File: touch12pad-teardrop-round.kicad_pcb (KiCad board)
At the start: 2 copper layers, 158.8 x 33 mm, 38 parts, among them J1 Conn_01x01_Female, J10 Conn_01x01_Female, J11 Conn_01x01_Female, J12 Conn_01x01_Female, J13 Conn_01x01_Female, J14 Conn_01x01_Female, J15 Conn_01x01_Female, J16 Conn_01x01_Female, J17 Conn_01x01_Female, J18 Conn_01x01_Female, J19 Conn_01x01_Female, J2 Conn_01x01_Female, J20 Conn_01x01_Female, J21 Conn_01x01_Female, J22 Conn_01x01_Female, J23 Conn_01x01_Female, J24 Conn_01x01_Female, J3 Conn_01x01_Female, J4 \, J5 Conn_01x01_Female, J6 Conn_01x01_Female, J7 Conn_01x01_Female, J8 Conn_01x01_Female, J9 Conn_01x01_Female

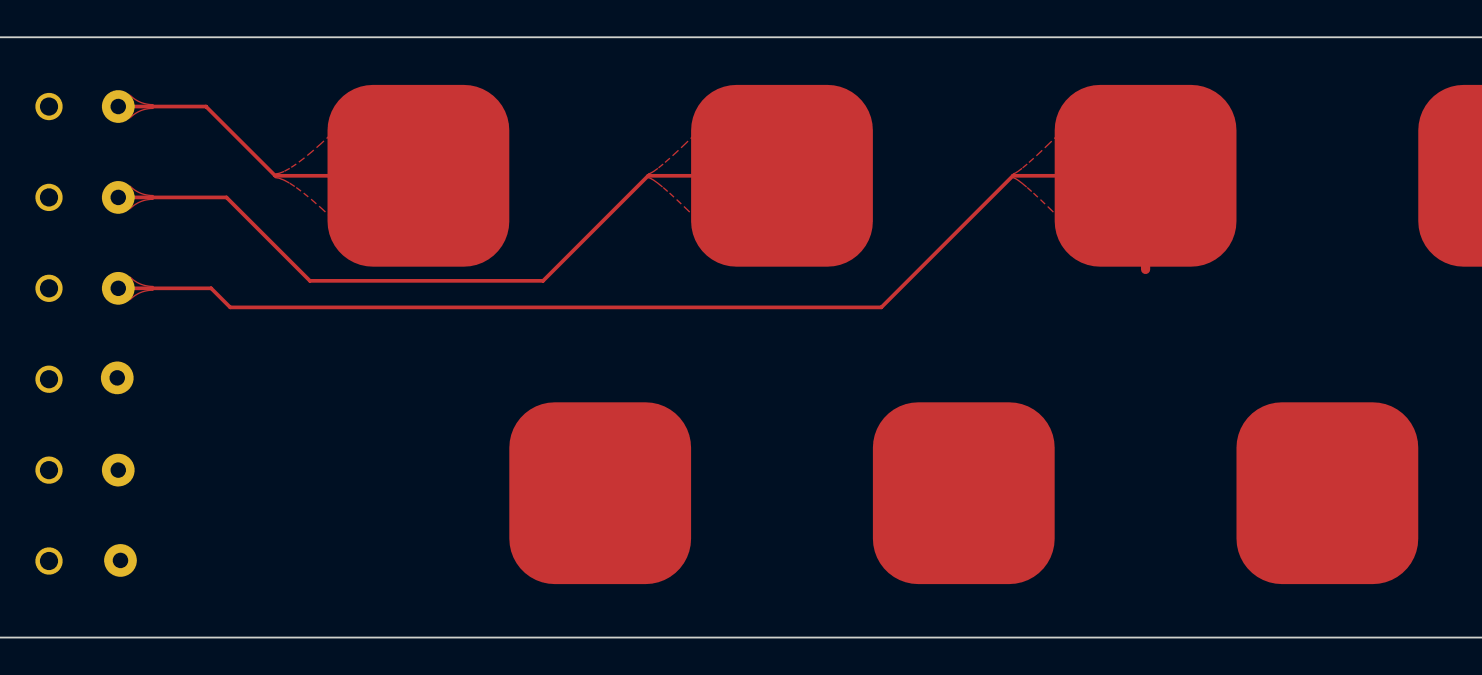
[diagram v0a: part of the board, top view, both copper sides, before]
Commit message: start re-routing flex touch board
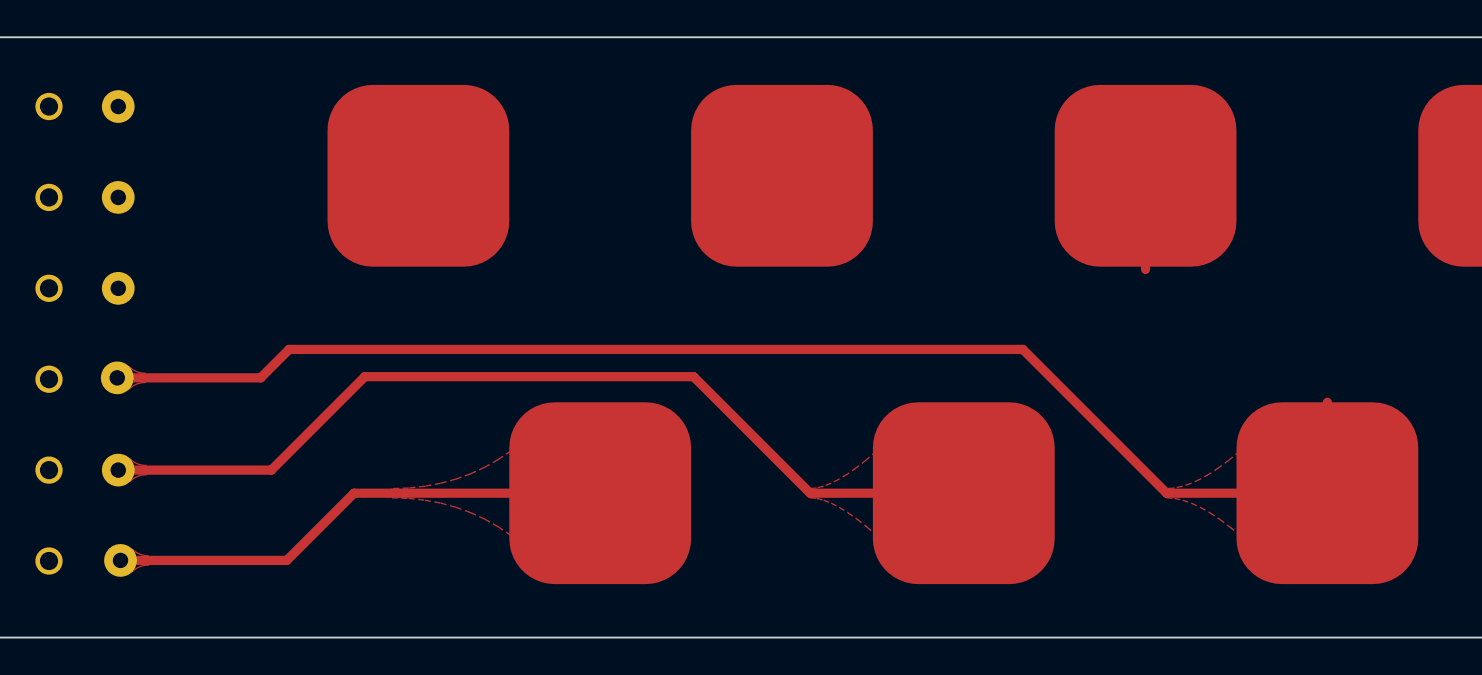
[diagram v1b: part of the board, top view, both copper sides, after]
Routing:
- net Net-(J12-Pad1): track 0.00 -> 75.5 mm
- net Net-(J9-Pad1): track 65.1 -> 5.15 mm
- net Net-(J11-Pad1): track 0.00 -> 51.3 mm
- net Net-(J8-Pad1): track 40.8 -> 0.00 mm
- net Net-(J10-Pad1): track 0.00 -> 27.9 mm
- net Net-(J1-Pad1): track 18.1 -> 0.04 mm
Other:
- net class Default: clearance 0.1524 -> 0.508; trace_width 0.1524 -> 0.508
- net class trace: clearance 0.254 -> 0.508
- rule trace_clearance: 0.1524 -> 0.508

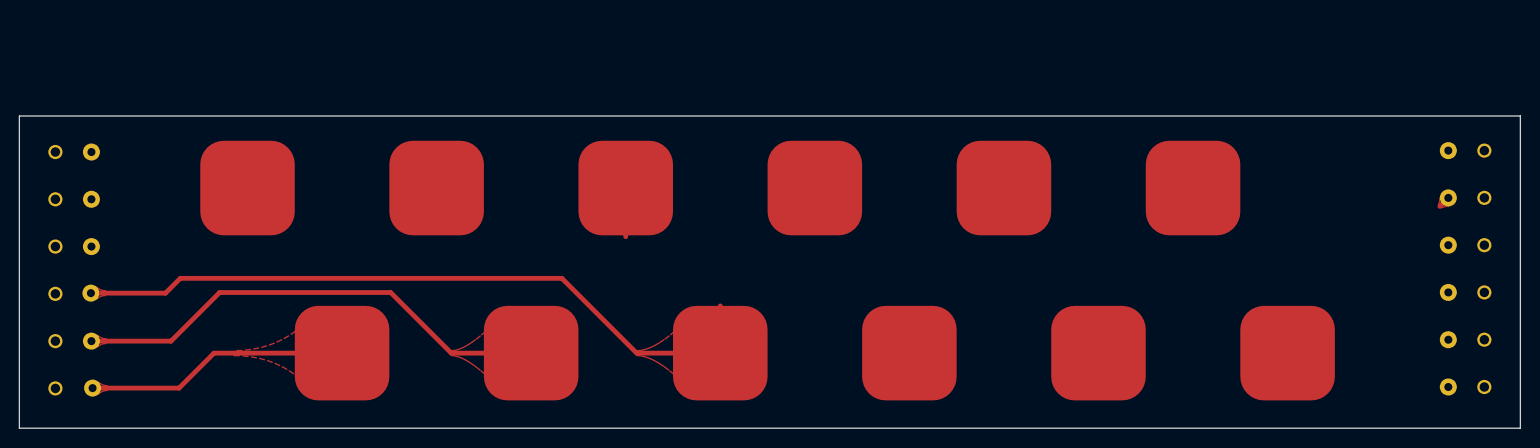
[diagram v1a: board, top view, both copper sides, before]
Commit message: add rounded tracks using plugin
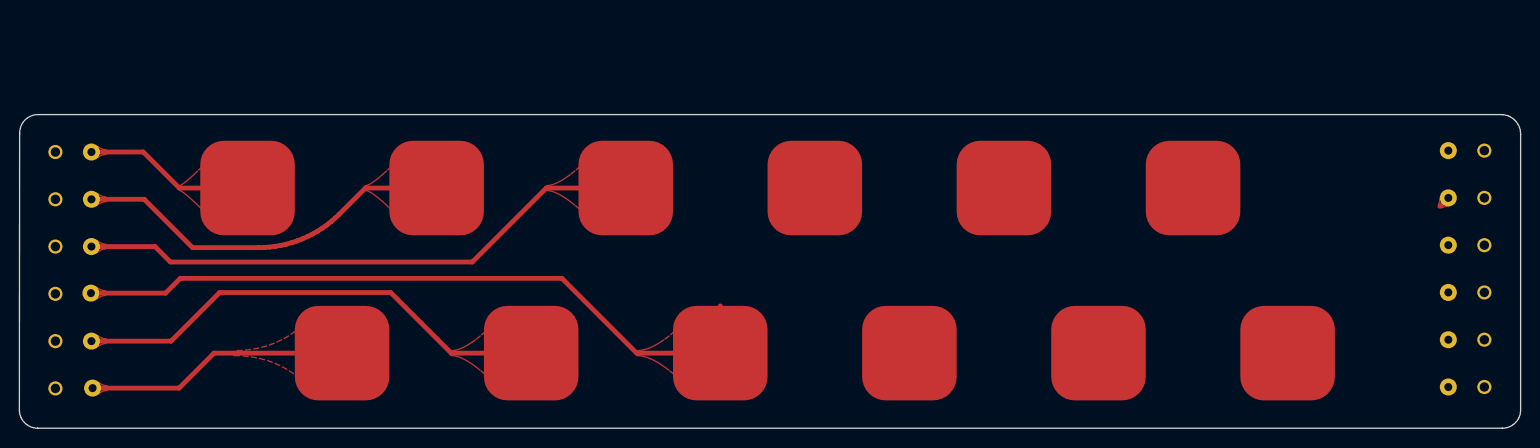
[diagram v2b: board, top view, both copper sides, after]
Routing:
- net Net-(J9-Pad1): track 5.15 -> 60.4 mm
- net Net-(J8-Pad1): track 0.00 -> 40.7 mm
- net Net-(J1-Pad1): track 0.04 -> 18.1 mm
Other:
- board size 158.8 x 33 mm -> 158.8 x 33.2 mm

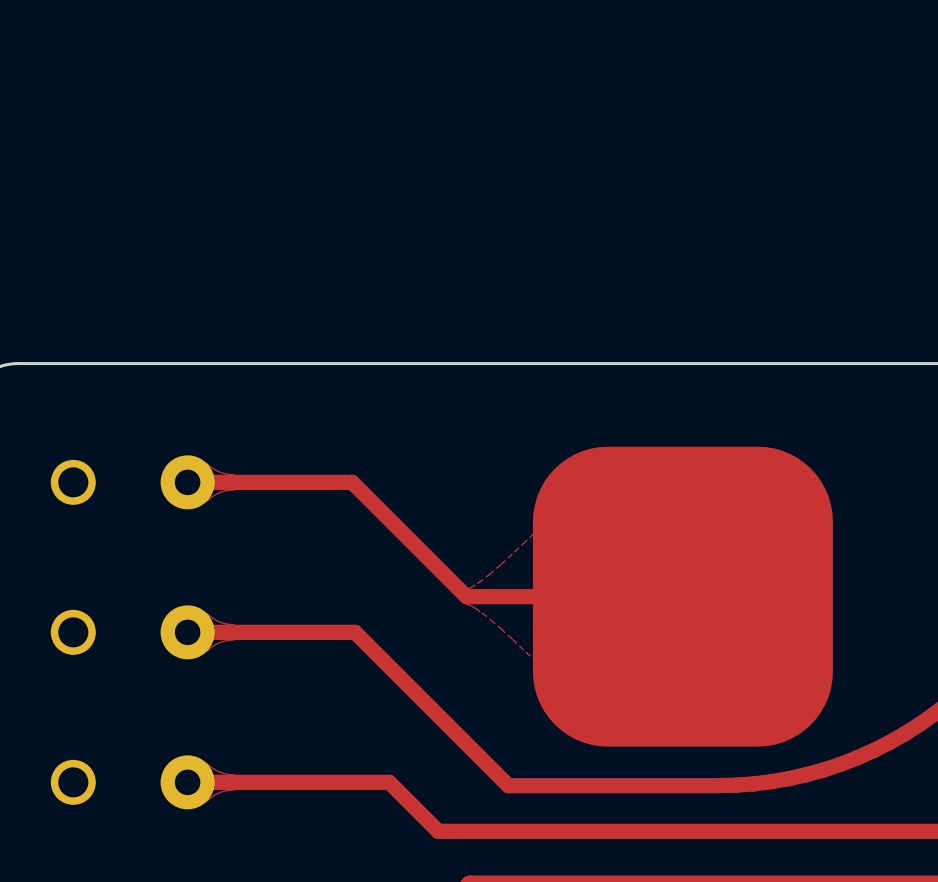
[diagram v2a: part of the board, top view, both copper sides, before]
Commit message: improve round traces with plugin
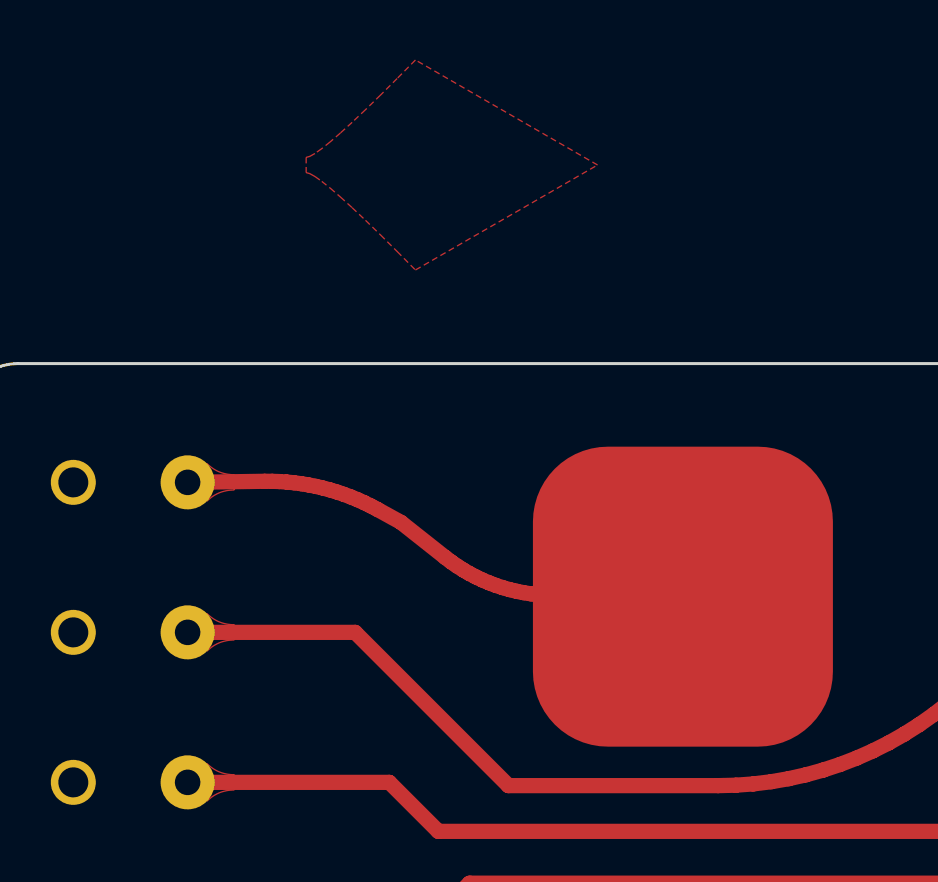
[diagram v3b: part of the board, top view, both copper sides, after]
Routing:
- net Net-(J1-Pad1): track 18.1 -> 17.5 mm
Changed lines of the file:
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@@
     (thickness 1.6)
     (drawings 12)
-    (tracks 45)
+    (tracks 78)
     (zones 0)
     (modules 38)
@@
   )
   (segment (start 34.29 17.78) (end 34.3154 17.8054) (width 0.508) (layer F.Cu) (net 1))
-  (segment (start 27.0764 17.78) (end 34.29 17.78) (width 0.508) (layer F.Cu) (net 1))
-  (segment (start 17.78 13.97) (end 23.2664 13.97) (width 0.508) (layer F.Cu) (net 1))
-  (segment (start 23.2664 13.97) (end 27.0764 17.78) (width 0.508) (layer F.Cu) (net 1))
+  (segment (start 20.352192 13.934275) (end 17.78 13.97) (width 0.508) (layer F.Cu) (net 1))
+  (segment (start 20.352192 13.934275) (end 20.596593 13.934827) (width 0.508) (layer F.Cu) (net 1))
+  (segment (start 20.596593 13.934827) (end 20.840848 13.94327) (width 0.508) (layer F.Cu) (net 1))
+  (segment (start 20.840848 13.94327) (end 21.084704 13.959597) (width 0.508) (layer F.Cu) (net 1))
+  (segment (start 21.084704 13.959597) (end 21.327906 13.983789) (width 0.508) (layer F.Cu) (net 1))
+  (segment (start 21.327906 13.983789) (end 21.570199 14.015821) (width 0.508) (layer F.Cu) (net 1))
+  (segment (start 21.570199 14.015821) (end 21.811332 14.055661) (width 0.508) (layer F.Cu) (net 1))
+  (segment (start 21.811332 14.055661) (end 22.051053 14.103265) (width 0.508) (layer F.Cu) (net 1))
+  (segment (start 22.051053 14.103265) (end 22.289111 14.158586) (width 0.508) (layer F.Cu) (net 1))
+  (segment (start 22.289111 14.158586) (end 22.525259 14.221565) (width 0.508) (layer F.Cu) (net 1))
+  (segment (start 22.525259 14.221565) (end 22.75925 14.292136) (width 0.508) (layer F.Cu) (net 1))
+  (segment (start 22.75925 14.292136) (end 22.990841 14.370226) (width 0.508) (layer F.Cu) (net 1))
+  (segment (start 22.990841 14.370226) (end 23.219789 14.455753) (width 0.508) (layer F.Cu) (net 1))
+  (segment (start 23.219789 14.455753) (end 23.445856 14.548628) (width 0.508) (layer F.Cu) (net 1))
+  (segment (start 23.445856 14.548628) (end 23.668807 14.648755) (width 0.508) (layer F.Cu) (net 1))
+  (segment (start 23.668807 14.648755) (end 23.888408 14.756029) (width 0.508) (layer F.Cu) (net 1))
+  (segment (start 23.888408 14.756029) (end 24.104431 14.870337) (width 0.508) (layer F.Cu) (net 1))
+  (segment (start 24.104431 14.870337) (end 24.892 15.3035) (width 0.508) (layer F.Cu) (net 1))
+  (segment (start 29.9399 17.736499) (end 34.29 17.78) (width 0.508) (layer F.Cu) (net 1))
+  (segment (start 29.9399 17.736499) (end 29.699161 17.729126) (width 0.508) (layer F.Cu) (net 1))
+  (segment (start 29.699161 17.729126) (end 29.458931 17.711838) (width 0.508) (layer F.Cu) (net 1))
+  (segment (start 29.458931 17.711838) (end 29.219617 17.684663) (width 0.508) (layer F.Cu) (net 1))
+  (segment (start 29.219617 17.684663) (end 28.981627 17.647648) (width 0.508) (layer F.Cu) (net 1))
+  (segment (start 28.981627 17.647648) (end 28.745365 17.600855) (width 0.508) (layer F.Cu) (net 1))
+  (segment (start 28.745365 17.600855) (end 28.511232 17.544365) (width 0.508) (layer F.Cu) (net 1))
+  (segment (start 28.511232 17.544365) (end 28.279626 17.478272) (width 0.508) (layer F.Cu) (net 1))
+  (segment (start 28.279626 17.478272) (end 28.050941 17.40269) (width 0.508) (layer F.Cu) (net 1))
+  (segment (start 28.050941 17.40269) (end 27.825566 17.317747) (width 0.508) (layer F.Cu) (net 1))
+  (segment (start 27.825566 17.317747) (end 27.603883 17.223587) (width 0.508) (layer F.Cu) (net 1))
+  (segment (start 27.603883 17.223587) (end 27.38627 17.12037) (width 0.508) (layer F.Cu) (net 1))
+  (segment (start 27.38627 17.12037) (end 27.173095 17.008271) (width 0.508) (layer F.Cu) (net 1))
+  (segment (start 27.173095 17.008271) (end 26.964722 16.887482) (width 0.508) (layer F.Cu) (net 1))
+  (segment (start 26.964722 16.887482) (end 26.761504 16.758207) (width 0.508) (layer F.Cu) (net 1))
+  (segment (start 26.761504 16.758207) (end 26.563788 16.620666) (width 0.508) (layer F.Cu) (net 1))
+  (segment (start 26.563788 16.620666) (end 26.371908 16.475094) (width 0.508) (layer F.Cu) (net 1))
+  (segment (start 26.371908 16.475094) (end 24.892 15.3035) (width 0.508) (layer F.Cu) (net 1))
   (segment (start 46.7614 17.78) (end 54.29 17.78) (width 0.508) (layer F.Cu) (net 8))
   (segment (start 17.78 18.97) (end 23.3642 18.97) (width 0.508) (layer F.Cu) (net 8))
@@
     (polygon
       (pts
-        (xy 27.0764 18.034) (xy 27.195839 18.066459) (xy 27.369689 18.163839) (xy 27.597951 18.326139) (xy 27.880623 18.553359)
-        (xy 28.217706 18.845499) (xy 28.6092 19.202559) (xy 29.055105 19.624539) (xy 29.555421 20.111439) (xy 30.110148 20.663259)
-        (xy 30.719286 21.28) (xy 36.79 17.78) (xy 30.719286 14.28) (xy 30.110148 14.89674) (xy 29.555421 15.44856)
-        (xy 29.055105 15.93546) (xy 28.6092 16.35744) (xy 28.217706 16.7145) (xy 27.880623 17.00664) (xy 27.597951 17.23386)
-        (xy 27.369689 17.39616) (xy 27.195839 17.49354) (xy 27.0764 17.526)
+        (xy 21.731252 3.64526) (xy 21.850691 3.677719) (xy 22.024541 3.775099) (xy 22.252803 3.937399) (xy 22.535475 4.164619)
+        (xy 22.872558 4.456759) (xy 23.264052 4.813819) (xy 23.709957 5.235799) (xy 24.210273 5.722699) (xy 24.765 6.274519)
+        (xy 25.374138 6.89126) (xy 31.444852 3.39126) (xy 25.374138 -0.10874) (xy 24.765 0.508) (xy 24.210273 1.05982)
+        (xy 23.709957 1.54672) (xy 23.264052 1.9687) (xy 22.872558 2.32576) (xy 22.535475 2.6179) (xy 22.252803 2.84512)
+        (xy 22.024541 3.00742) (xy 21.850691 3.1048) (xy 21.731252 3.13726)
       )
     )

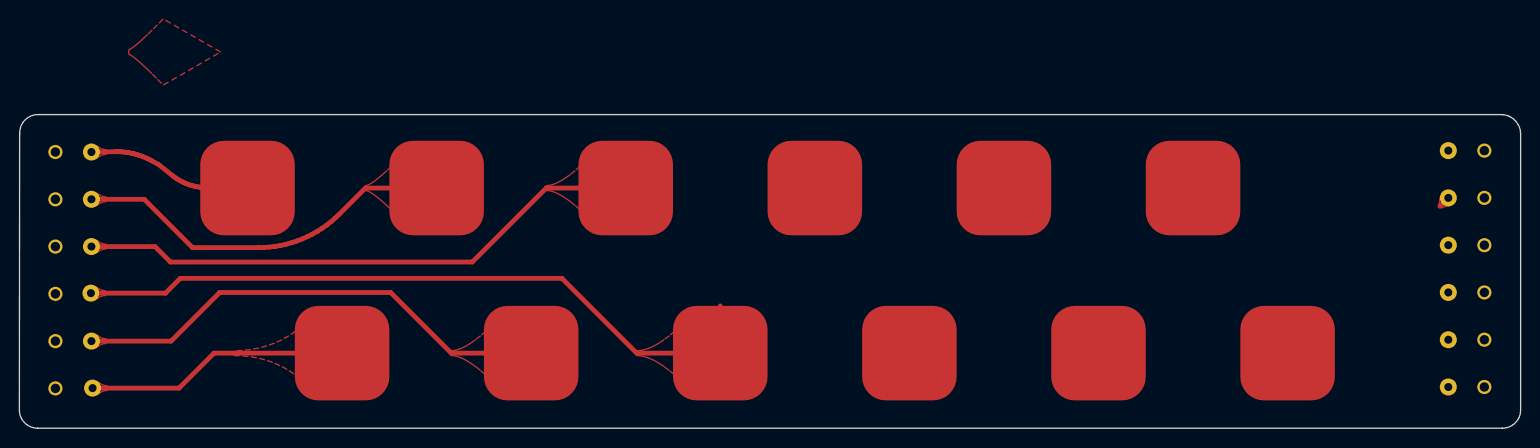
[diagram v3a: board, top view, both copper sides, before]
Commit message: update round tracks
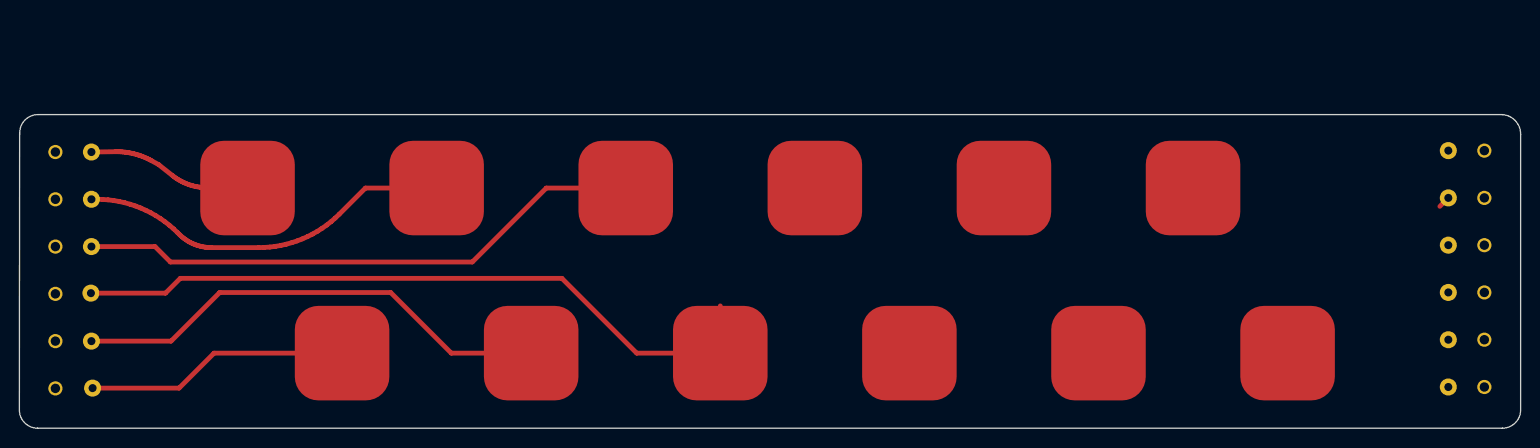
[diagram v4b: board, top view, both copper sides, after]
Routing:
- net Net-(J8-Pad1): track 40.7 -> 40.0 mm

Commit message: add more round tracks
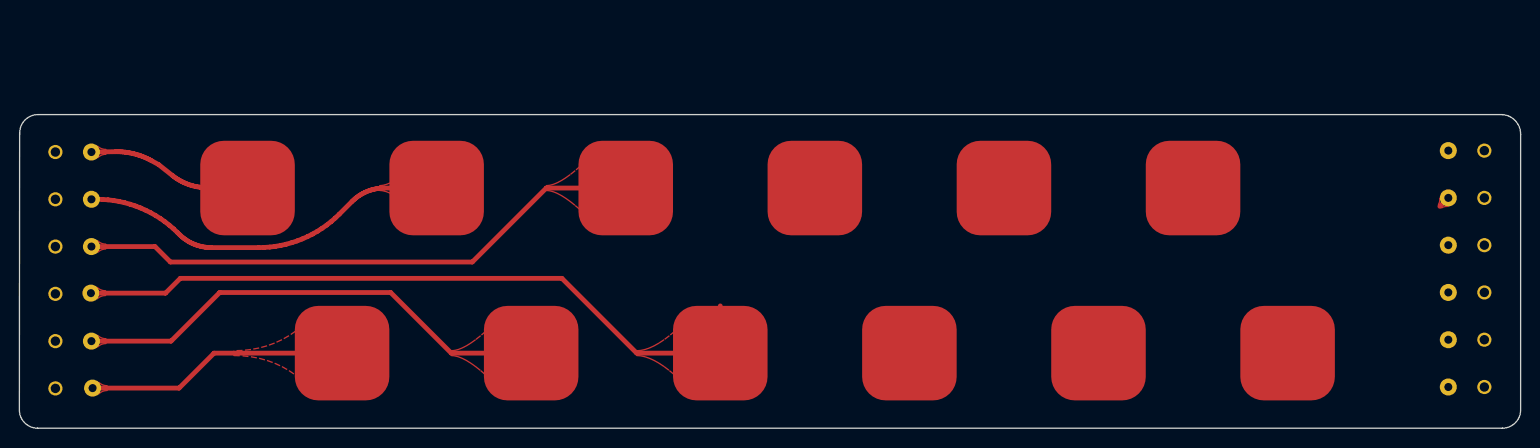
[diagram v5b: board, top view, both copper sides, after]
